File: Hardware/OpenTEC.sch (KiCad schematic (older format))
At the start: 69 parts, among them J1 USB_B_Micro, J10 TEMP3, J11 TEC, J12 XH2.54, J13 XH2.54, J14 XH2.54, J15 XH2.54, J16 XH2.54, J17 XH2.54, J18 XH2.54, J19 XH2.54, J2 4P Screw Terminal, J20 XH2.54, J21 XH2.54, J22 XH2.54, J23 XH2.54, J24 XH2.54, J25 XH2.54, J26 XH2.54, J27 XH2.54, J3 10P JTAG/SWD, J4 LCD, J5 I2C, J6 BOOT_SEL, J7 TEMP0, J8 TEMP1, J9 TEMP2, Q1 FDS6574A, Q2 FDS6574A, Q3 FDS6574A, Q4 FDS6574A, U1 AMS1117-5.0, U11 STM32F103C8T6, U2 AMS1117-3.3, U3 IR2104, U4 IR2104, Y1 16MHz

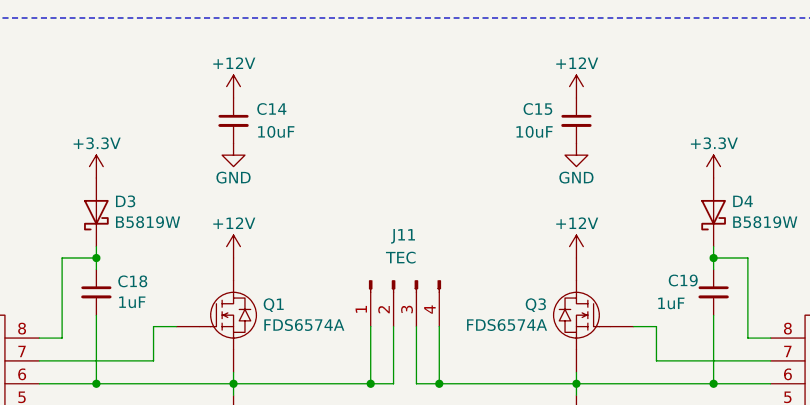
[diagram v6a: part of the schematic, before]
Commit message: Add BFC to H-bridge
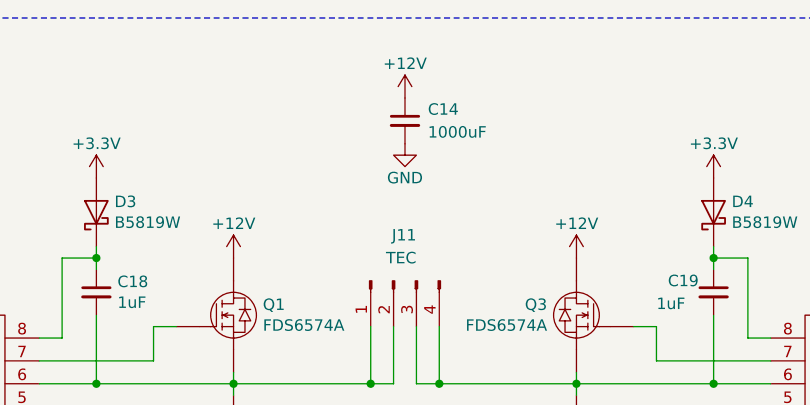
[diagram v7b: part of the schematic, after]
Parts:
- removed C15: 10uF, Capacitor_SMD:C_0805_2012Metric, symbol Device:C_Small
- C14: value 10uF -> 1000uF; footprint Capacitor_SMD:C_0805_2012Metric -> Capacitor_THT:CP_Radial_D13.0mm_P5.00mm
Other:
- moved on the sheet: C14
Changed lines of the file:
@@
-$EndComp
-$Comp
-L Device:C_Small C15
-U 1 1 60285BBA
-P 9100 950
-F 0 "C15" H 9200 1000 50  0000 L CNN
-F 1 "10uF" H 9200 900 50  0000 L CNN
-F 2 "Capacitor_SMD:C_0805_2012Metric" H 9100 950 50  0001 C CNN
-F 3 "~" H 9100 950 50  0001 C CNN
-	1    9100 950
-	-1   0    0    -1
-$EndComp
-$Comp
-L power:GND #PWR05
-U 1 1 60285BC0
-P 9100 1050
-F 0 "#PWR05" H 9100 800 50  0001 C CNN
-F 1 "GND" H 9100 900 50  0000 C CNN
-F 2 "" H 9100 1050 50  0001 C CNN
-F 3 "" H 9100 1050 50  0001 C CNN
-	1    9100 1050
-	-1   0    0    -1
-$EndComp
-$Comp
-L power:+12V #PWR02
-U 1 1 602876F3
-P 9100 850
-F 0 "#PWR02" H 9100 700 50  0001 C CNN
-F 1 "+12V" H 9100 1000 50  0000 C CNN
-F 2 "" H 9100 850 50  0001 C CNN
-F 3 "" H 9100 850 50  0001 C CNN
-	1    9100 850
-	1    0    0    -1
 $EndComp
 $Comp
 L Device:C_Small C14
 U 1 1 6028A22D
-P 7600 950
-F 0 "C14" H 7700 1000 50  0000 L CNN
-F 1 "10uF" H 7700 900 50  0000 L CNN
-F 2 "Capacitor_SMD:C_0805_2012Metric" H 7600 950 50  0001 C CNN
-F 3 "~" H 7600 950 50  0001 C CNN
-	1    7600 950
+P 8350 950
+F 0 "C14" H 8450 1000 50  0000 L CNN
+F 1 "1000uF" H 8450 900 50  0000 L CNN
+F 2 "Capacitor_THT:CP_Radial_D13.0mm_P5.00mm" H 8350 950 50  0001 C CNN
+F 3 "~" H 8350 950 50  0001 C CNN
+	1    8350 950
 	1    0    0    -1
 $EndComp
@@
 L power:GND #PWR04
 U 1 1 6028A233
-P 7600 1050
-F 0 "#PWR04" H 7600 800 50  0001 C CNN
-F 1 "GND" H 7600 900 50  0000 C CNN
-F 2 "" H 7600 1050 50  0001 C CNN
-F 3 "" H 7600 1050 50  0001 C CNN
-	1    7600 1050
+P 8350 1050
+F 0 "#PWR04" H 8350 800 50  0001 C CNN
+F 1 "GND" H 8350 900 50  0000 C CNN
+F 2 "" H 8350 1050 50  0001 C CNN
+F 3 "" H 8350 1050 50  0001 C CNN
+	1    8350 1050
 	1    0    0    -1
 $EndComp
@@
 L power:+12V #PWR01
 U 1 1 6028DA69
-P 7600 850
-F 0 "#PWR01" H 7600 700 50  0001 C CNN
-F 1 "+12V" H 7600 1000 50  0000 C CNN
-F 2 "" H 7600 850 50  0001 C CNN
-F 3 "" H 7600 850 50  0001 C CNN
-	1    7600 850
+P 8350 850
+F 0 "#PWR01" H 8350 700 50  0001 C CNN
+F 1 "+12V" H 8350 1000 50  0000 C CNN
+F 2 "" H 8350 850 50  0001 C CNN
+F 3 "" H 8350 850 50  0001 C CNN
+	1    8350 850
 	1    0    0    -1
 $EndComp

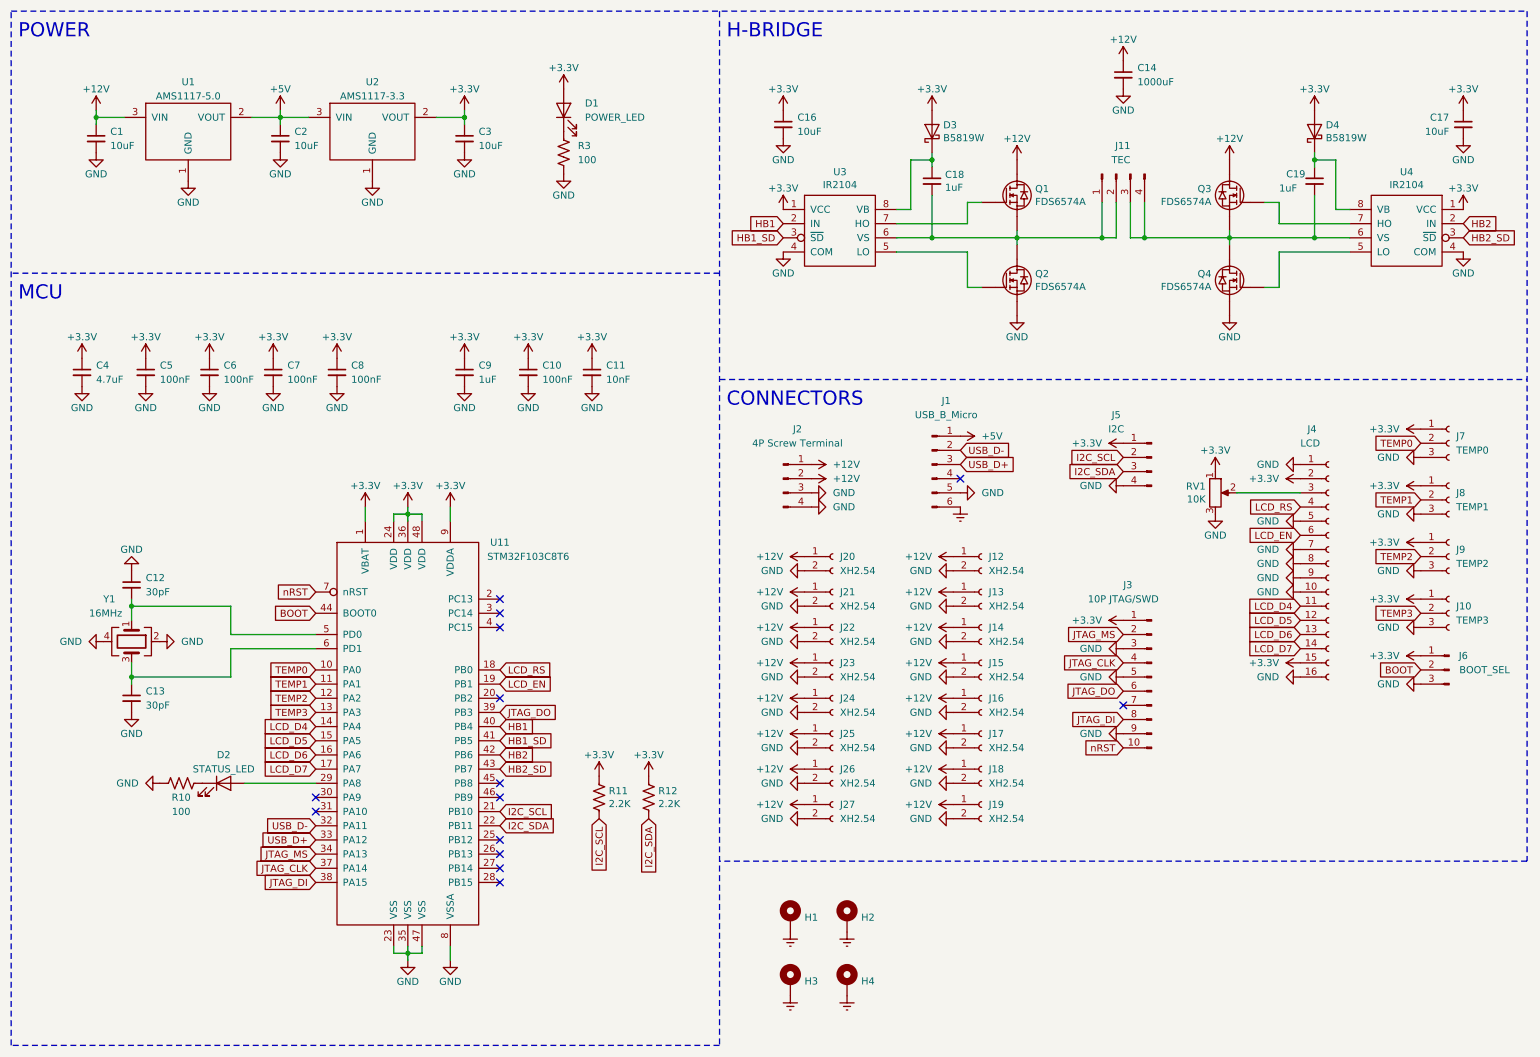
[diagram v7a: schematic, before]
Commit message: Remove unused USB port and 5V LDO
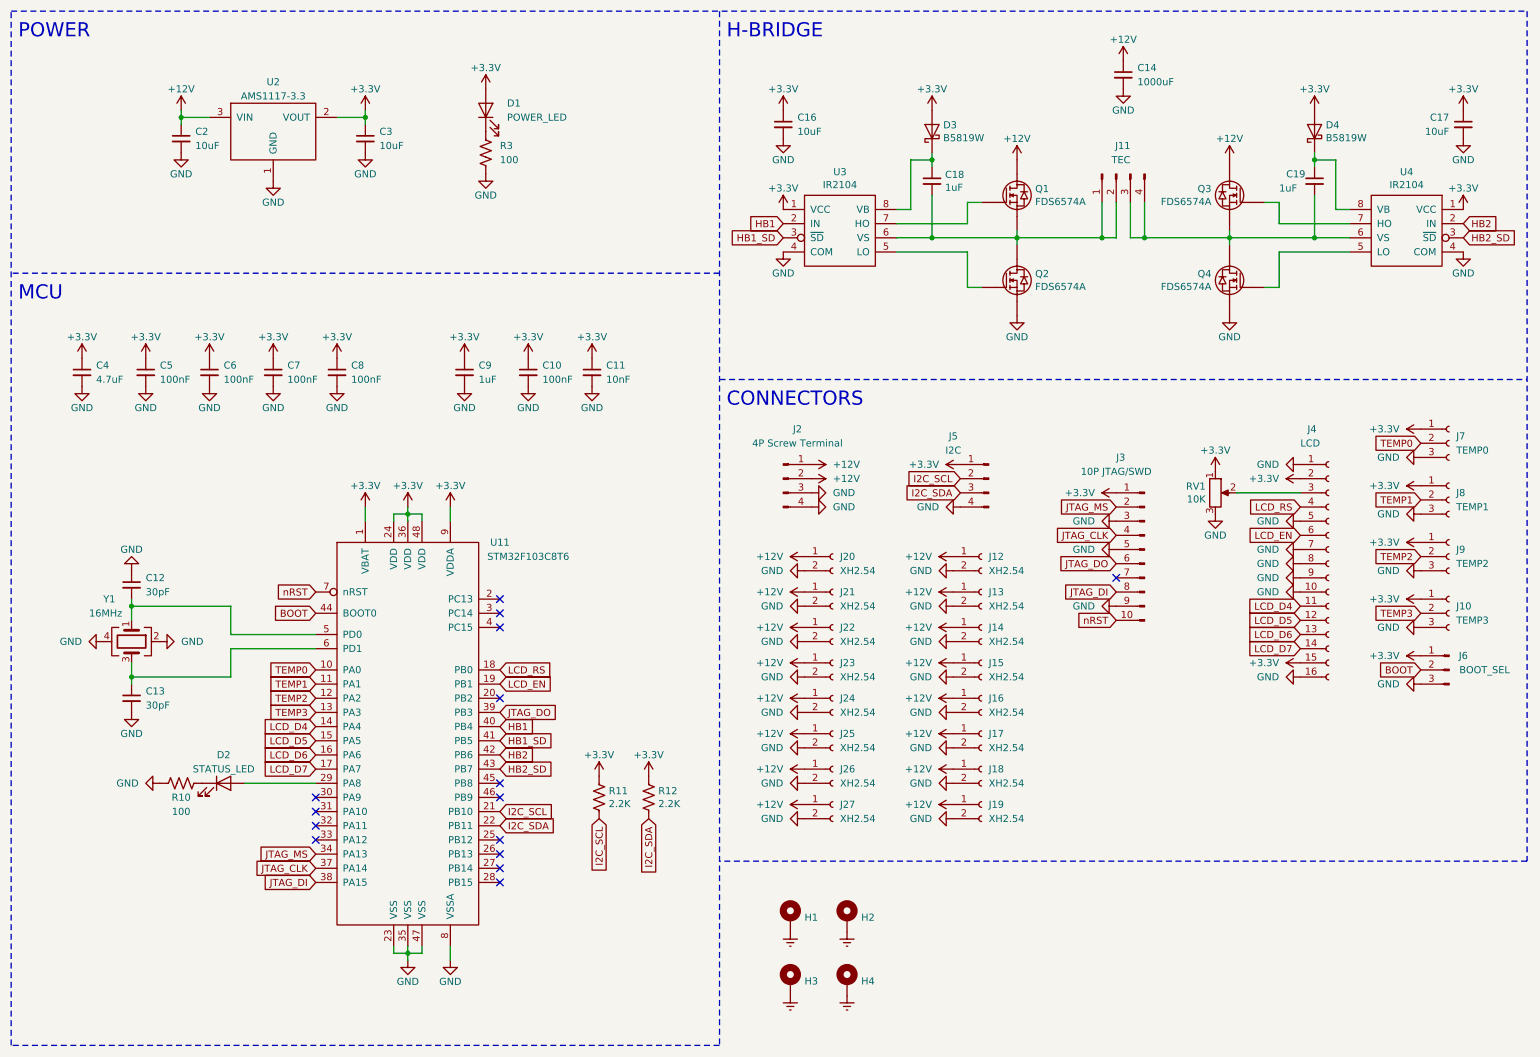
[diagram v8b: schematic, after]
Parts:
- removed C1: 10uF, Capacitor_SMD:C_0805_2012Metric, symbol Device:C_Small
- removed J1: USB_B_Micro, Connector_USB:USB_Micro-B_Amphenol_10103594-0001LF_Horizontal, symbol Connector:Conn_01x06_Male
- removed U1: AMS1117-5.0, Package_TO_SOT_SMD:SOT-223-3_TabPin2, symbol OpenTEC:AMS1117
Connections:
- net +5V is gone; now on net +12V: C2.1, U2.3 (VIN)
- net USB_D+: no longer names the net of U11.33 (PA12)
- net USB_D-: no longer names the net of U11.32 (PA11)
- no-connect marks 14 -> 15
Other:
- moved on the sheet: C2, C3, D1, J3, J5, R3, U2
